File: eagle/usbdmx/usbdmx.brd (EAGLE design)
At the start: 63.2 x 50.2 mm, 33 parts, among them IC1 MAX3468CSA, IC2 MAX3468CSA, Q1 16MHz

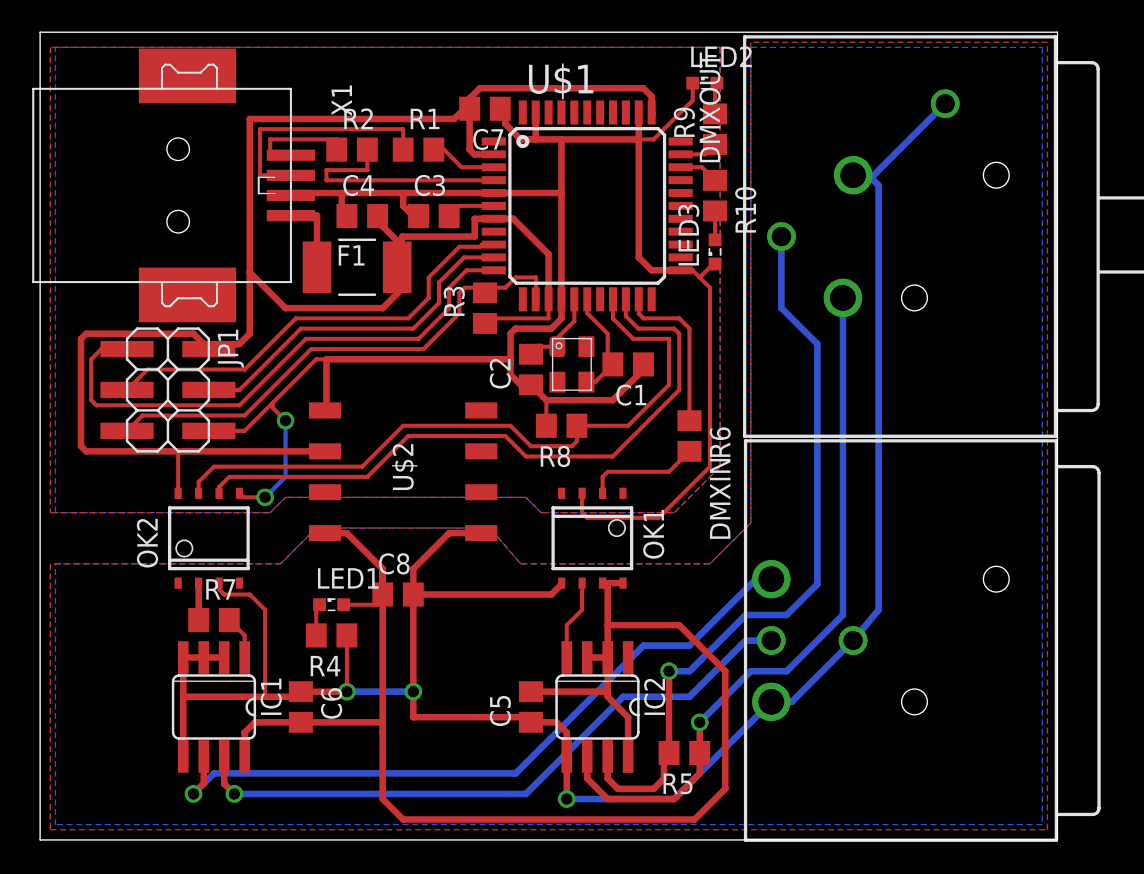
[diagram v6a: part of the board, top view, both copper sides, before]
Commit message: replace the optocoupler package
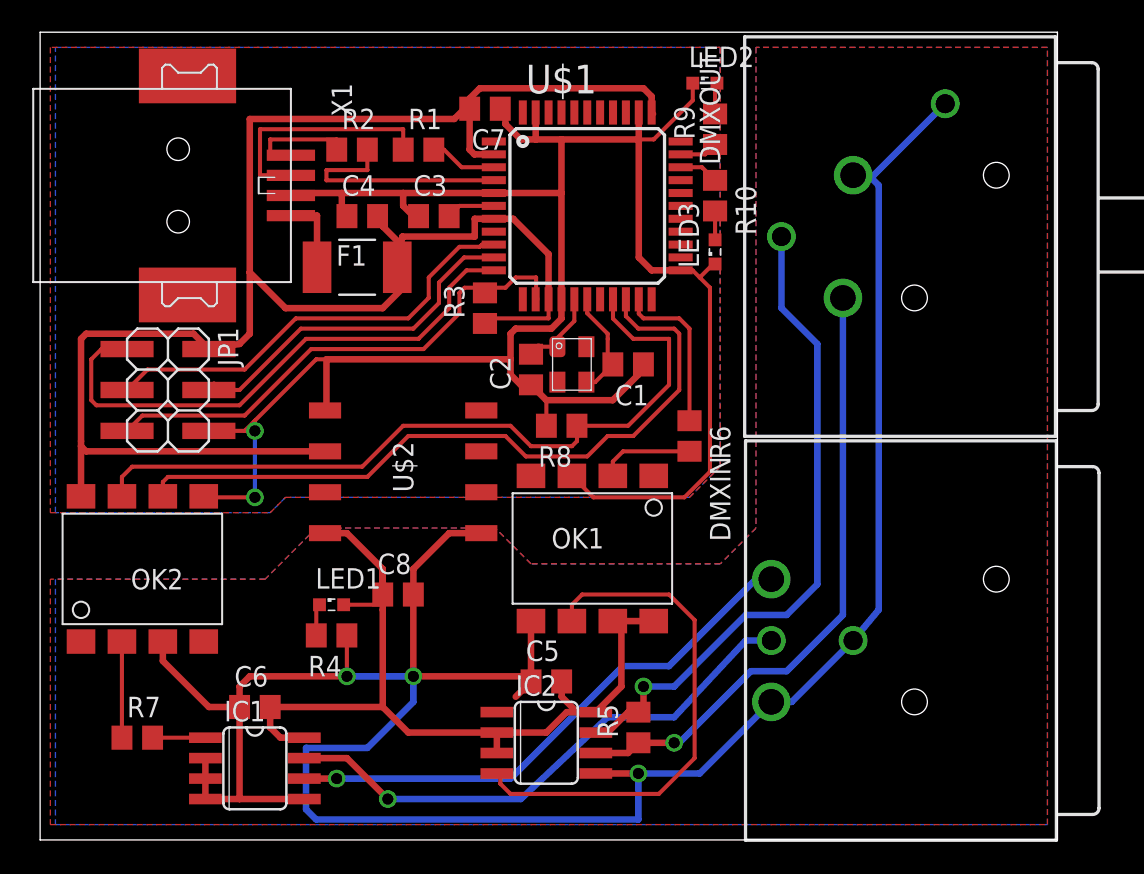
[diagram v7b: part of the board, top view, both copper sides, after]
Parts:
- OK1, OK2: value 6N137SO-8 -> 6N137SMD-8; device optocoupler:SO-8 -> optocoupler:SMD8
- moved R7 8.72 mm to (6.03, 6.35)
- moved IC1 4.58 mm to (13.3, 4.45), turned to 270 degrees
- moved OK2 4.55 mm to (6.35, 16.8)
- moved IC2 3.88 mm to (31.4, 6.03), turned to 270 degrees
- moved R5 3.27 mm to (37.1, 6.99), turned to 90 degrees
- moved C6 2.86 mm to (13.3, 8.26), turned to 0 degrees
- moved C5 1.85 mm to (31.4, 9.84), turned to 0 degrees
- moved OK1 0.64 mm to (34.3, 18.1)
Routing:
- net SVCC: track 90.5 -> 56.5 mm
- net N$20: track 5.01 -> 32.1 mm
- net SGND: track 132.8 -> 154.5 mm
- net N$18: track 44.0 -> 34.1 mm
- net N$29: track 39.9 -> 34.1 mm
- net N$12: track 44.1 -> 38.6 mm
- net N$17: track 46.1 -> 40.8 mm
- net N$16: track 42.1 -> 47.2 mm
- net N$24: track 40.8 -> 44.7 mm
- net N$23: track 2.29 -> 5.97 mm
- net N$25: track 7.08 -> 5.92 mm
- net GND: track 136.0 -> 135.1 mm
- net N$21: track 2.72 -> 3.28 mm
- net VCC: track 120.4 -> 120.9 mm

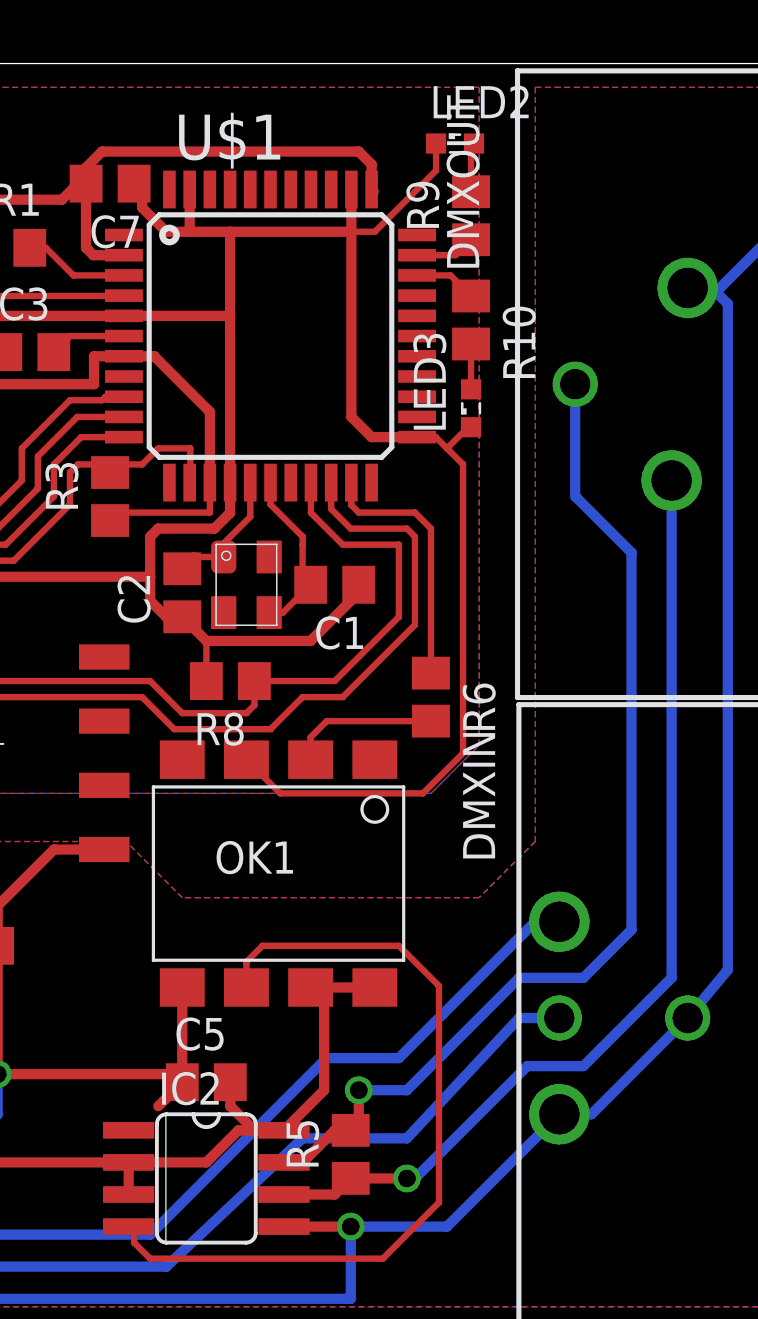
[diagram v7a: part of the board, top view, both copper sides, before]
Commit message: add a solder pad to enable the boot loader
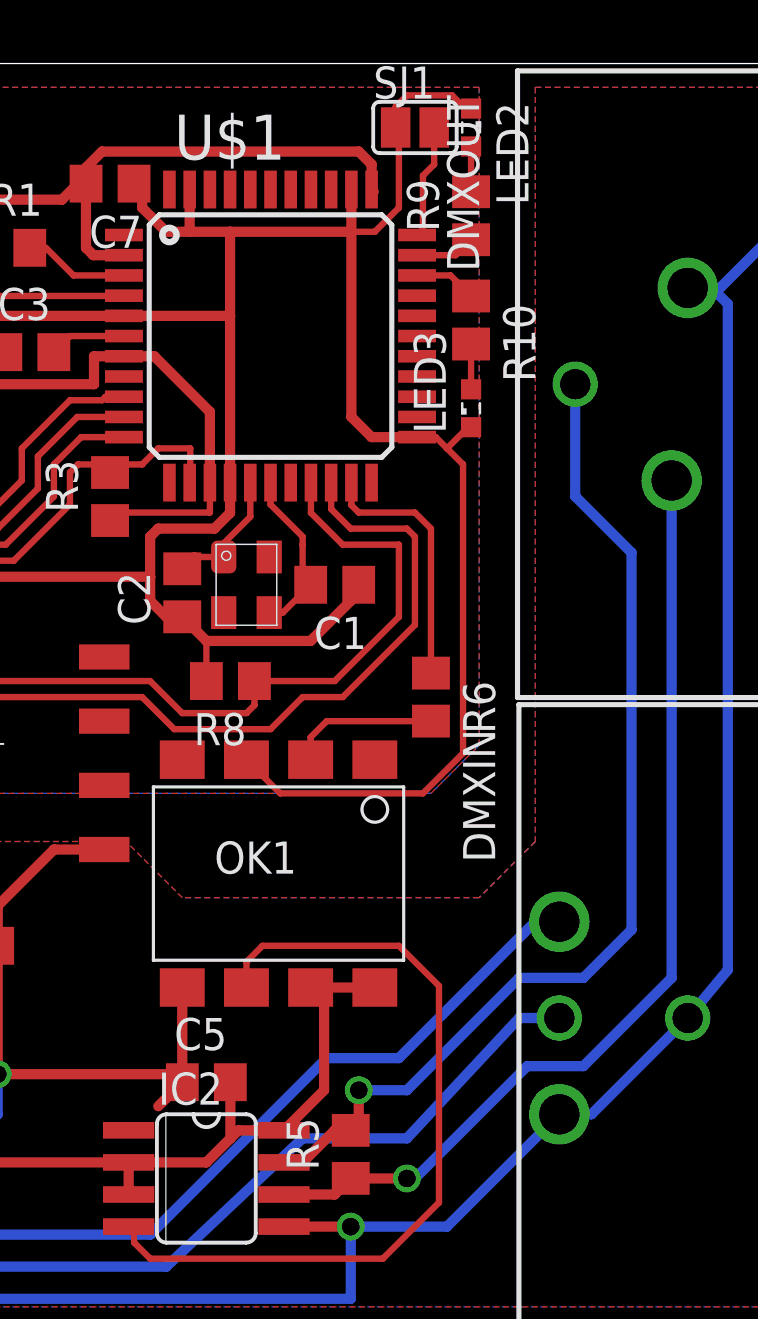
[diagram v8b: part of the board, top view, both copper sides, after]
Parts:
- added SJ1: (no value), jumper:SJ
- moved LED2 0.90 mm to (41.9, 47.6), turned to 270 degrees
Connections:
- new net N$19: SJ1.2, U$1.33
- net GND: now also SJ1.1
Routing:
- net N$19: track 0.00 -> 4.54 mm
- net GND: track 135.1 -> 139.5 mm
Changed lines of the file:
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@@
 <element name="R9" library="rcl" package="R0805" value="220" x="41.91" y="44.1325" rot="R90"/>
 <element name="R10" library="rcl" package="R0805" value="220" x="41.91" y="40.005" rot="R270"/>
-<element name="LED2" library="led" package="SML0603" value="" x="41.275" y="46.99"/>
+<element name="LED2" library="led" package="SML0603" value="" x="41.91" y="47.625" rot="R270"/>
 <element name="LED3" library="led" package="SML0603" value="" x="41.91" y="36.5125" rot="R90"/>
+<element name="SJ1" library="jumper" package="SJ" value="" x="39.6875" y="47.625"/>
 </elements>
 <signals>
@@
 <contactref element="LED3" pad="C"/>
 <wire x1="38.1" y1="43.4975" x2="37.1725" y2="43.4975" width="0.254" layer="1"/>
-<wire x1="40.525" y1="46.99" x2="40.525" y2="45.9225" width="0.254" layer="1"/>
-<wire x1="40.525" y1="45.9225" x2="38.1" y2="43.4975" width="0.254" layer="1"/>
 <wire x1="41.91" y1="35.7625" x2="41.795" y2="35.7625" width="0.254" layer="1"/>
 <wire x1="41.795" y1="35.7625" x2="40.9575" y2="34.925" width="0.254" layer="1"/>
@@
 <wire x1="34.3535" y1="21.2725" x2="40.005" y2="21.2725" width="0.254" layer="1"/>
 <wire x1="40.005" y1="21.2725" x2="41.5925" y2="22.86" width="0.254" layer="1"/>
+<contactref element="SJ1" pad="1"/>
+<wire x1="41.91" y1="48.375" x2="41.795" y2="48.26" width="0.254" layer="1"/>
+<wire x1="41.795" y1="48.26" x2="41.16" y2="48.895" width="0.254" layer="1"/>
+<wire x1="41.16" y1="48.895" x2="39.37" y2="48.895" width="0.254" layer="1"/>
+<wire x1="39.37" y1="48.895" x2="38.9255" y2="48.4505" width="0.254" layer="1"/>
+<wire x1="38.9255" y1="48.4505" x2="38.9255" y2="47.625" width="0.254" layer="1"/>
+<wire x1="38.9255" y1="47.625" x2="39.0525" y2="47.498" width="0.254" layer="1"/>
+<wire x1="39.0525" y1="47.498" x2="39.0525" y2="44.45" width="0.254" layer="1"/>
+<wire x1="39.0525" y1="44.45" x2="38.1" y2="43.4975" width="0.254" layer="1"/>
 </signal>
 <signal name="N$2">
@@
 <wire x1="36.195" y1="13.589" x2="35.56" y2="13.589" width="0.4064" layer="1"/>
 <wire x1="34.5059" y1="7.9375" x2="33.3375" y2="7.9375" width="0.4064" layer="1"/>
-<wire x1="33.3375" y1="7.9375" x2="32.385" y2="8.89" width="0.4064" layer="1"/>
-<wire x1="32.385" y1="8.89" x2="32.385" y2="9.84" width="0.4064" layer="1"/>
 <wire x1="32.385" y1="9.84" x2="32.3825" y2="9.8425" width="0.4064" layer="1"/>
 <wire x1="35.875" y1="13.274" x2="35.56" y2="13.589" width="0.4064" layer="1"/>
@@
 <wire x1="21.275" y1="8.255" x2="22.8625" y2="6.6675" width="0.4064" layer="1"/>
 <wire x1="22.8625" y1="6.6675" x2="28.3591" y2="6.6675" width="0.4064" layer="1"/>
-<wire x1="31.4325" y1="6.6675" x2="32.7025" y2="7.9375" width="0.4064" layer="1"/>
+<wire x1="31.4325" y1="6.6675" x2="32.385" y2="7.62" width="0.4064" layer="1"/>
+<wire x1="32.385" y1="7.62" x2="32.7025" y2="7.9375" width="0.4064" layer="1"/>
 <wire x1="32.7025" y1="7.9375" x2="34.5059" y2="7.9375" width="0.4064" layer="1"/>
+<wire x1="32.385" y1="9.84" x2="32.385" y2="7.62" width="0.4064" layer="1"/>
 </signal>
 <signal name="SGND">
@@
 <contactref element="R9" pad="2"/>
 <wire x1="41.91" y1="45.0825" x2="41.91" y2="46.875" width="0.254" layer="1"/>
-<wire x1="41.91" y1="46.875" x2="42.025" y2="46.99" width="0.254" layer="1"/>
 </signal>
 <signal name="N$27">
@@
 <wire x1="18.415" y1="3.81" x2="29.21" y2="3.81" width="0.4064" layer="16"/>
 </signal>
+<signal name="N$19">
+<contactref element="U$1" pad="33"/>
+<contactref element="SJ1" pad="2"/>
+<wire x1="39.7725" y1="43.37" x2="40.005" y2="43.6025" width="0.254" layer="1"/>
+<wire x1="40.005" y1="43.6025" x2="40.005" y2="45.72" width="0.254" layer="1"/>
+<wire x1="40.005" y1="45.72" x2="40.4495" y2="46.1645" width="0.254" layer="1"/>
+<wire x1="40.4495" y1="46.1645" x2="40.4495" y2="47.625" width="0.254" layer="1"/>
+</signal>
 </signals>
